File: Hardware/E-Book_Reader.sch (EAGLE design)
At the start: 103 parts, among them IC1 BD5229G-TR, IC4 XC6220A331MR-G, J1 FH34SRJ-24S-0.5SH_99_, J2 SAMACSYS_PARTS_USB4110-GF-A, J3 QWIIC_RIGHT_ANGLE, J4 112A-TAAR-R03_ATTEND, Q1 20V/4.2A/52mΩ/1.4W, Q2 20V/4.2A/52mΩ/1.4W, Q3 SI1308EDL-T1-GE3, U1 MAX17048G+T10, U2 ESP32-C6-WROOM-1-N8, U3 W25Q512JVEIQ, U4 DS3231SN#

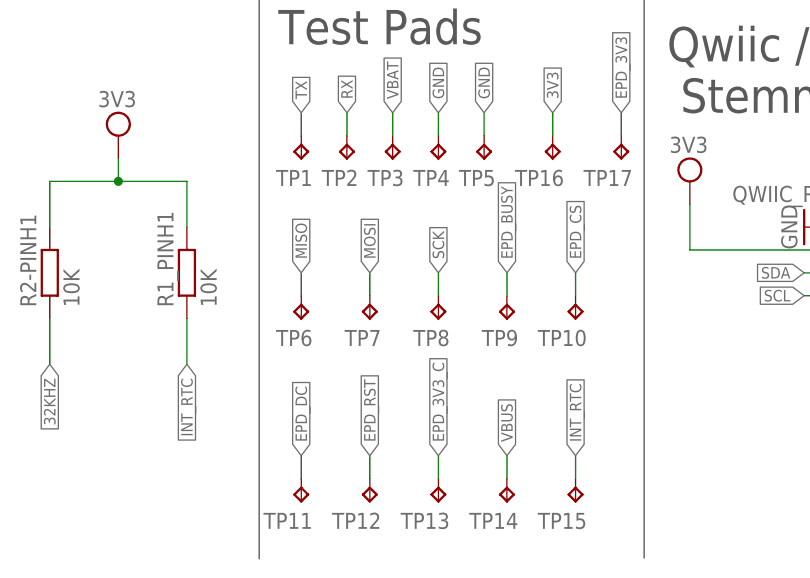
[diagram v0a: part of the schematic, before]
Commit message: Updated Schematic and PCB After Fixing Issues
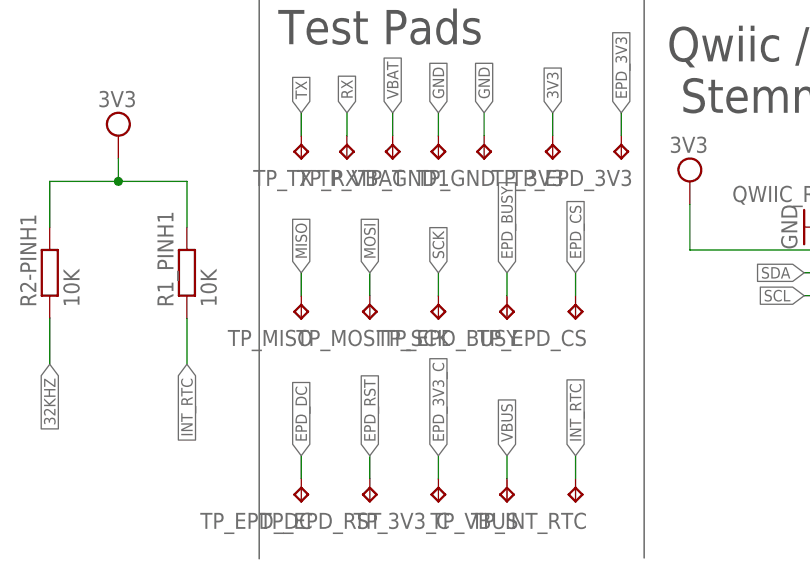
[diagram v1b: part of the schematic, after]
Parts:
- renumbered TP1 to TP_TX, TP10 to TP_EPD_CS, TP11 to TP_EPD_DC, TP12 to TP_EPD_RST, TP13 to TP_3V3_C, TP14 to TP_VBUS, TP15 to TP_INT_RTC, TP16 to TP_3V3, TP17 to TP_EPD_3V3, TP2 to TP_RX, TP3 to TP_VBAT, TP4 to TP_GND1, TP5 to TP_GND, TP6 to TP_MISO, TP7 to TP_MOSI, TP8 to TP_SCK, TP9 to TP_EPD_BUSY
